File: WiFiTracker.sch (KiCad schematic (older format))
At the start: 30 parts, among them IC1 CP2104, P1 ANT, P2 Battery, P3 USB_B, Q1 MMBT2222A, Q2 MMBT2222A, SW1 SW_RESET, U1 RFM95W-868S2, U2 AP2114, U3 MCP73831T-2ATI/OT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

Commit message: Check PCB V0.1
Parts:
- P3: symbol USB_B -> USB_B-RESCUE-WiFiTracker
- U1: footprint TIH:XCVR_RFM95W-868S2 -> rfm95:XCVR_RFM95W-868S2
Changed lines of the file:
@@
 GPIO0
 $Comp
-L USB_B P3
+L USB_B-RESCUE-WiFiTracker P3
 U 1 1 58AB3572
 P 4320 5825
@@
 F 0 "U1" H 1490 2230 50  0000 L CNN
 F 1 "RFM95W-868S2" H 1490 980 50  0000 L CNN
-F 2 "TIH:XCVR_RFM95W-868S2" H 2090 1680 50  0001 L CNN
+F 2 "rfm95:XCVR_RFM95W-868S2" H 2090 1680 50  0001 L CNN
 F 3 "Mod Txrx Lora +20dbm 868mhz Smd" H 2090 1680 50  0001 L CNN
 F 4 "22.89 USD" H 2090 1680 50  0001 L CNN "Price"

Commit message: Added pin DIOs
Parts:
- added D6, D7, D8: D, symbol D
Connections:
- net RST_RN is gone; now on net RESET: U4.4 (GPIO16)
- net SCL is gone; now on net GPIO5: U4.20 (GPIO5)
- net SRX is gone; now on net GPIO12: U4.6 (GPIO12)
- net STX is gone; now on net GPIO14: U4.5 (GPIO14)
- net GPIO15: now also D6.1 (K), D7.1 (K), D8.1 (K)
- net DIO0: now reaches U1.14 (DIO0)
- net DIO0: now also D7.2 (A)
- net DIO1: now reaches U1.15 (DIO1)
- net DIO1: now also D8.2 (A)
- net DIO2: now reaches U1.16 (DIO2)
- net DIO2: now also D6.2 (A)
- net GPIO16 renamed GPIO5
- net SDA renamed GPIO4
- no-connect marks 27 -> 25
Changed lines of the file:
@@
 $EndComp
 $Comp
-L GND #PWR01
+L GND #PWR5
 U 1 1 58AB3534
 P 995 5905
-F 0 "#PWR01" H 995 5655 50  0001 C CNN
+F 0 "#PWR5" H 995 5655 50  0001 C CNN
 F 1 "GND" H 995 5755 50  0000 C CNN
 F 2 "" H 995 5905 50  0000 C CNN
@@
 $EndComp
 $Comp
-L +3.3V #PWR02
+L +3.3V #PWR7
 U 1 1 58AB3536
 P 2895 5305
-F 0 "#PWR02" H 2895 5155 50  0001 C CNN
+F 0 "#PWR7" H 2895 5155 50  0001 C CNN
 F 1 "+3.3V" H 2895 5445 50  0000 C CNN
 F 2 "" H 2895 5305 50  0000 C CNN
@@
 $EndComp
 $Comp
-L VCC #PWR03
+L VCC #PWR1
 U 1 1 58AB3537
 P 595 4855
-F 0 "#PWR03" H 595 4705 50  0001 C CNN
+F 0 "#PWR1" H 595 4705 50  0001 C CNN
 F 1 "VCC" H 595 5005 50  0000 C CNN
 F 2 "" H 595 4855 50  0000 C CNN
@@
 $EndComp
 $Comp
-L +BATT #PWR04
+L +BATT #PWR4
 U 1 1 58AB3538
 P 695 5005
-F 0 "#PWR04" H 695 4855 50  0001 C CNN
+F 0 "#PWR4" H 695 4855 50  0001 C CNN
 F 1 "+BATT" H 695 5145 50  0000 C CNN
 F 2 "" H 695 5005 50  0000 C CNN
@@
 $EndComp
 $Comp
-L GND #PWR05
+L GND #PWR10
 U 1 1 58AB353B
 P 3285 7405
-F 0 "#PWR05" H 3285 7155 50  0001 C CNN
+F 0 "#PWR10" H 3285 7155 50  0001 C CNN
 F 1 "GND" H 3285 7255 50  0000 C CNN
 F 2 "" H 3285 7405 50  0000 C CNN
@@
 $EndComp
 $Comp
-L VCC #PWR06
+L VCC #PWR2
 U 1 1 58AB353C
 P 685 6655
-F 0 "#PWR06" H 685 6505 50  0001 C CNN
+F 0 "#PWR2" H 685 6505 50  0001 C CNN
 F 1 "VCC" H 685 6805 50  0000 C CNN
 F 2 "" H 685 6655 50  0000 C CNN
@@
 $EndComp
 $Comp
-L +BATT #PWR07
+L +BATT #PWR11
 U 1 1 58AB3540
 P 3585 6605
-F 0 "#PWR07" H 3585 6455 50  0001 C CNN
+F 0 "#PWR11" H 3585 6455 50  0001 C CNN
 F 1 "+BATT" H 3585 6745 50  0000 C CNN
 F 2 "" H 3585 6605 50  0000 C CNN
@@
 $EndComp
 $Comp
-L GND #PWR08
+L GND #PWR12
 U 1 1 58AB3541
 P 3635 7155
-F 0 "#PWR08" H 3635 6905 50  0001 C CNN
+F 0 "#PWR12" H 3635 6905 50  0001 C CNN
 F 1 "GND" H 3635 7005 50  0000 C CNN
 F 2 "" H 3635 7155 50  0000 C CNN
@@
 $EndComp
 $Comp
-L GND #PWR09
+L GND #PWR3
 U 1 1 58AB3544
 P 685 7355
-F 0 "#PWR09" H 685 7105 50  0001 C CNN
+F 0 "#PWR3" H 685 7105 50  0001 C CNN
 F 1 "GND" H 685 7205 50  0000 C CNN
 F 2 "" H 685 7355 50  0000 C CNN
@@
 $EndComp
 $Comp
-L GND #PWR010
+L GND #PWR20
 U 1 1 58AB354A
 P 8030 3810
-F 0 "#PWR010" H 8030 3560 50  0001 C CNN
+F 0 "#PWR20" H 8030 3560 50  0001 C CNN
 F 1 "GND" H 8030 3660 50  0000 C CNN
 F 2 "" H 8030 3810 50  0000 C CNN
@@
 $EndComp
 $Comp
-L +3.3V #PWR011
+L +3.3V #PWR21
 U 1 1 58AB354C
 P 8930 3160
-F 0 "#PWR011" H 8930 3010 50  0001 C CNN
+F 0 "#PWR21" H 8930 3010 50  0001 C CNN
 F 1 "+3.3V" H 8930 3300 50  0000 C CNN
 F 2 "" H 8930 3160 50  0000 C CNN
@@
 BATTERY AND SOURCE
 $Comp
-L GND #PWR012
+L GND #PWR6
 U 1 1 58AB355C
 P 2795 5805
-F 0 "#PWR012" H 2795 5555 50  0001 C CNN
+F 0 "#PWR6" H 2795 5555 50  0001 C CNN
 F 1 "GND" H 2795 5655 50  0000 C CNN
 F 2 "" H 2795 5805 50  0000 C CNN
@@
 RXD
 Text Label 9925 1385 0    60   ~ 0
-SCL
+GPIO5
 Text Label 9925 1485 0    60   ~ 0
-SDA
+GPIO4
 NoConn ~ 8955 2385
 NoConn ~ 8855 2385
@@
 CH_PD
 Text Label 7590 1485 2    60   ~ 0
-RST_RN
+RESET
 Text Label 7625 1585 2    60   ~ 0
-STX
+GPIO14
 Text Label 7605 1685 2    60   ~ 0
-SRX
+GPIO12
 Text Label 7615 1785 0    60   ~ 0
 GPIO13
@@
 RESET
 $Comp
-L GND #PWR013
+L GND #PWR22
 U 1 1 58AB355F
 P 9925 1885
-F 0 "#PWR013" H 9925 1635 50  0001 C CNN
+F 0 "#PWR22" H 9925 1635 50  0001 C CNN
 F 1 "GND" H 9925 1735 50  0000 C CNN
 F 2 "" H 9925 1885 50  0000 C CNN
@@
 $EndComp
 $Comp
-L +3.3V #PWR014
+L +3.3V #PWR18
 U 1 1 58AB3560
 P 7425 1885
-F 0 "#PWR014" H 7425 1735 50  0001 C CNN
+F 0 "#PWR18" H 7425 1735 50  0001 C CNN
 F 1 "+3.3V" H 7425 2025 50  0000 C CNN
 F 2 "" H 7425 1885 50  0000 C CNN
@@
 $EndComp
 $Comp
-L GND #PWR015
+L GND #PWR24
 U 1 1 58AB3563
 P 10575 4240
-F 0 "#PWR015" H 10575 3990 50  0001 C CNN
+F 0 "#PWR24" H 10575 3990 50  0001 C CNN
 F 1 "GND" H 10575 4090 50  0000 C CNN
 F 2 "" H 10575 4240 50  0000 C CNN
@@
 $EndComp
 $Comp
-L +3.3V #PWR016
+L +3.3V #PWR23
 U 1 1 58AB3564
 P 10275 3580
-F 0 "#PWR016" H 10275 3430 50  0001 C CNN
+F 0 "#PWR23" H 10275 3430 50  0001 C CNN
 F 1 "+3.3V" H 10275 3720 50  0000 C CNN
 F 2 "" H 10275 3580 50  0000 C CNN
@@
 GPIO2
 $Comp
-L +3.3V #PWR017
+L +3.3V #PWR25
 U 1 1 58AB356D
 P 10895 3565
-F 0 "#PWR017" H 10895 3415 50  0001 C CNN
+F 0 "#PWR25" H 10895 3415 50  0001 C CNN
 F 1 "+3.3V" H 10895 3705 50  0000 C CNN
 F 2 "" H 10895 3565 50  0000 C CNN
@@
 $EndComp
 $Comp
-L +3.3V #PWR018
+L +3.3V #PWR19
 U 1 1 58AB3571
 P 7495 4085
-F 0 "#PWR018" H 7495 3935 50  0001 C CNN
+F 0 "#PWR19" H 7495 3935 50  0001 C CNN
 F 1 "+3.3V" H 7495 4225 50  0000 C CNN
 F 2 "" H 7495 4085 50  0000 C CNN
@@
 NoConn ~ 5075 6420
 $Comp
-L +3.3V #PWR019
+L +3.3V #PWR15
 U 1 1 58AB3574
 P 4855 6215
-F 0 "#PWR019" H 4855 6065 50  0001 C CNN
+F 0 "#PWR15" H 4855 6065 50  0001 C CNN
 F 1 "+3.3V" H 4855 6355 50  0000 C CNN
 F 2 "" H 4855 6215 50  0000 C CNN
@@
 $EndComp
 $Comp
-L GND #PWR020
+L GND #PWR16
 U 1 1 58AB3576
 P 4905 6550
-F 0 "#PWR020" H 4905 6300 50  0001 C CNN
+F 0 "#PWR16" H 4905 6300 50  0001 C CNN
 F 1 "GND" H 4905 6400 50  0000 C CNN
 F 2 "" H 4905 6550 50  0000 C CNN
@@
 NoConn ~ 6475 6320
 $Comp
-L GND #PWR021
+L GND #PWR17
 U 1 1 58AB3577
 P 5010 7110
-F 0 "#PWR021" H 5010 6860 50  0001 C CNN
+F 0 "#PWR17" H 5010 6860 50  0001 C CNN
 F 1 "GND" H 5010 6960 50  0000 C CNN
 F 2 "" H 5010 7110 50  0000 C CNN
@@
 RST
 $Comp
-L VCC #PWR022
+L VCC #PWR13
 U 1 1 58AB3578
 P 4575 6245
-F 0 "#PWR022" H 4575 6095 50  0001 C CNN
+F 0 "#PWR13" H 4575 6095 50  0001 C CNN
 F 1 "VCC" H 4575 6395 50  0000 C CNN
 F 2 "" H 4575 6245 50  0000 C CNN
@@
 $EndComp
 $Comp
-L GND #PWR023
+L GND #PWR14
 U 1 1 58AB3579
 P 4785 5590
-F 0 "#PWR023" H 4785 5340 50  0001 C CNN
+F 0 "#PWR14" H 4785 5340 50  0001 C CNN
 F 1 "GND" H 4785 5440 50  0000 C CNN
 F 2 "" H 4785 5590 50  0000 C CNN
@@
 GPIO14
 Text Label 1180 1480 2    60   ~ 0
-GPIO16
-$Comp
-L GND #PWR024
+GPIO5
+$Comp
+L GND #PWR8
 U 1 1 58AB7D79
 P 2960 2370
-F 0 "#PWR024" H 2960 2120 50  0001 C CNN
+F 0 "#PWR8" H 2960 2120 50  0001 C CNN
 F 1 "GND" H 2960 2220 50  0000 C CNN
 F 2 "" H 2960 2370 50  0000 C CNN
@@
 $EndComp
 $Comp
-L +3.3V #PWR025
+L +3.3V #PWR9
 U 1 1 58AB7DFC
 P 3040 1210
-F 0 "#PWR025" H 3040 1060 50  0001 C CNN
+F 0 "#PWR9" H 3040 1060 50  0001 C CNN
 F 1 "+3.3V" H 3040 1350 50  0000 C CNN
 F 2 "" H 3040 1210 50  0000 C CNN
@@
 	1    0    0    -1
 $EndComp
-NoConn ~ 1390 2180
-NoConn ~ 1390 2080
-NoConn ~ 1390 1980
 NoConn ~ 1390 1880
 NoConn ~ 1390 1780
@@
 	1    590  5200
 	0    -1   -1   0
+$EndComp
+NoConn ~ 2595 5755
+$Comp
+L CONN_01X01 P1
+U 1 1 58AC21D1
+P 3410 1480
+F 0 "P1" H 3410 1580 50  0000 C CNN
+F 1 "ANT" V 3510 1480 50  0000 C CNN
+F 2 "Connect:1pin" H 3410 1480 50  0001 C CNN
+F 3 "" H 3410 1480 50  0000 C CNN
+	1    3410 1480
+	1    0    0    -1
+$EndComp
+NoConn ~ 1645 5605
+Text Label 1285 1980 2    60   ~ 0
+DIO0
+Text Label 1285 2080 2    60   ~ 0
+DIO1
+Text Label 1280 2180 2    60   ~ 0
+DIO2
+NoConn ~ 1390 1580
+$Comp
+L D D8
+U 1 1 5940BAF2
+P 5705 935
+F 0 "D8" H 5705 1035 50  0000 C CNN
+F 1 "D" H 5705 835 50  0000 C CNN
+F 2 "" H 5705 935 50  0000 C CNN
+F 3 "" H 5705 935 50  0000 C CNN
+	1    5705 935
+	-1   0    0    1
+$EndComp
+$Comp
+L D D6
+U 1 1 5940BBBD
+P 5690 1205
+F 0 "D6" H 5690 1305 50  0000 C CNN
+F 1 "D" H 5690 1105 50  0000 C CNN
+F 2 "" H 5690 1205 50  0000 C CNN
+F 3 "" H 5690 1205 50  0000 C CNN
+	1    5690 1205
+	-1   0    0    1
+$EndComp
+$Comp
+L D D7
+U 1 1 5940BDF7
+P 5695 660
+F 0 "D7" H 5695 760 50  0000 C CNN
+F 1 "D" H 5695 560 50  0000 C CNN
+F 2 "" H 5695 660 50  0000 C CNN
+F 3 "" H 5695 660 50  0000 C CNN
+	1    5695 660
+	-1   0    0    1
 $EndComp
 Wire Wire Line
@@
 	5415 3255 5290 3255
 Wire Wire Line
-	5090 3255 4890 3255
+	4890 3255 5090 3255
 Wire Wire Line
 	5400 2630 5275 2630
 Wire Wire Line
-	5075 2630 4875 2630
+	4875 2630 5075 2630
 Wire Wire Line
 	5700 2830 5700 2915
@@
 	695  5355 695  5405
 Connection ~ 695  5405
-NoConn ~ 2595 5755
-$Comp
-L CONN_01X01 P1
-U 1 1 58AC21D1
-P 3410 1480
-F 0 "P1" H 3410 1580 50  0000 C CNN
-F 1 "ANT" V 3510 1480 50  0000 C CNN
-F 2 "Connect:1pin" H 3410 1480 50  0001 C CNN
-F 3 "" H 3410 1480 50  0000 C CNN
-	1    3410 1480
-	1    0    0    -1
-$EndComp
 Wire Wire Line
 	2790 1480 3210 1480
-NoConn ~ 1645 5605
+Wire Wire Line
+	1390 1980 1285 1980
+Wire Wire Line
+	1390 2080 1285 2080
+Wire Wire Line
+	1390 2180 1280 2180
+Wire Wire Line
+	5845 660  5965 660
+Wire Wire Line
+	5965 660  5965 1205
+Wire Wire Line
+	5965 1205 5840 1205
+Wire Wire Line
+	5855 935  6210 935
+Connection ~ 5965 935
+Wire Wire Line
+	5545 660  5370 660
+Wire Wire Line
+	5555 935  5380 935
+Wire Wire Line
+	5540 1205 5395 1205
+Text Label 5370 660  0    60   ~ 0
+DIO0
+Text Label 5380 935  0    60   ~ 0
+DIO1
+Text Label 5395 1205 0    60   ~ 0
+DIO2
+Text Label 6210 935  0    60   ~ 0
+GPIO15
 $EndSCHEMATC

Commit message: Update name
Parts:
- D6, D7, D8: footprint (none) -> Diodes_SMD:D_SOD-123F
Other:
- note added: "RFM95"
- note removed: "RN2903 LoRa"
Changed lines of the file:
@@
 Title "LoRaCat: WiFiTracker"
 Date "2017-02-20"
-Rev "0.1"
+Rev "0.2"
 Comp "Electronic Cats"
 Comment1 "Andres Sabas"
@@
 $EndComp
 $Comp
-L GND #PWR5
+L GND #PWR01
 U 1 1 58AB3534
 P 995 5905
-F 0 "#PWR5" H 995 5655 50  0001 C CNN
+F 0 "#PWR01" H 995 5655 50  0001 C CNN
 F 1 "GND" H 995 5755 50  0000 C CNN
 F 2 "" H 995 5905 50  0000 C CNN
@@
 $EndComp
 $Comp
-L +3.3V #PWR7
+L +3.3V #PWR02
 U 1 1 58AB3536
 P 2895 5305
-F 0 "#PWR7" H 2895 5155 50  0001 C CNN
+F 0 "#PWR02" H 2895 5155 50  0001 C CNN
 F 1 "+3.3V" H 2895 5445 50  0000 C CNN
 F 2 "" H 2895 5305 50  0000 C CNN
@@
 $EndComp
 $Comp
-L VCC #PWR1
+L VCC #PWR03
 U 1 1 58AB3537
 P 595 4855
-F 0 "#PWR1" H 595 4705 50  0001 C CNN
+F 0 "#PWR03" H 595 4705 50  0001 C CNN
 F 1 "VCC" H 595 5005 50  0000 C CNN
 F 2 "" H 595 4855 50  0000 C CNN
@@
 $EndComp
 $Comp
-L +BATT #PWR4
+L +BATT #PWR04
 U 1 1 58AB3538
 P 695 5005
-F 0 "#PWR4" H 695 4855 50  0001 C CNN
+F 0 "#PWR04" H 695 4855 50  0001 C CNN
 F 1 "+BATT" H 695 5145 50  0000 C CNN
 F 2 "" H 695 5005 50  0000 C CNN
@@
 $EndComp
 $Comp
-L GND #PWR10
+L GND #PWR05
 U 1 1 58AB353B
 P 3285 7405
-F 0 "#PWR10" H 3285 7155 50  0001 C CNN
+F 0 "#PWR05" H 3285 7155 50  0001 C CNN
 F 1 "GND" H 3285 7255 50  0000 C CNN
 F 2 "" H 3285 7405 50  0000 C CNN
@@
 $EndComp
 $Comp
-L VCC #PWR2
+L VCC #PWR06
 U 1 1 58AB353C
 P 685 6655
-F 0 "#PWR2" H 685 6505 50  0001 C CNN
+F 0 "#PWR06" H 685 6505 50  0001 C CNN
 F 1 "VCC" H 685 6805 50  0000 C CNN
 F 2 "" H 685 6655 50  0000 C CNN
@@
 $EndComp
 $Comp
-L +BATT #PWR11
+L +BATT #PWR07
 U 1 1 58AB3540
 P 3585 6605
-F 0 "#PWR11" H 3585 6455 50  0001 C CNN
+F 0 "#PWR07" H 3585 6455 50  0001 C CNN
 F 1 "+BATT" H 3585 6745 50  0000 C CNN
 F 2 "" H 3585 6605 50  0000 C CNN
@@
 $EndComp
 $Comp
-L GND #PWR12
+L GND #PWR08
 U 1 1 58AB3541
 P 3635 7155
-F 0 "#PWR12" H 3635 6905 50  0001 C CNN
+F 0 "#PWR08" H 3635 6905 50  0001 C CNN
 F 1 "GND" H 3635 7005 50  0000 C CNN
 F 2 "" H 3635 7155 50  0000 C CNN
@@
 $EndComp
 $Comp
-L GND #PWR3
+L GND #PWR09
 U 1 1 58AB3544
 P 685 7355
-F 0 "#PWR3" H 685 7105 50  0001 C CNN
+F 0 "#PWR09" H 685 7105 50  0001 C CNN
 F 1 "GND" H 685 7205 50  0000 C CNN
 F 2 "" H 685 7355 50  0000 C CNN
@@
 $EndComp
 $Comp
-L GND #PWR20
+L GND #PWR010
 U 1 1 58AB354A
 P 8030 3810
-F 0 "#PWR20" H 8030 3560 50  0001 C CNN
+F 0 "#PWR010" H 8030 3560 50  0001 C CNN
 F 1 "GND" H 8030 3660 50  0000 C CNN
 F 2 "" H 8030 3810 50  0000 C CNN
@@
 $EndComp
 $Comp
-L +3.3V #PWR21
+L +3.3V #PWR011
 U 1 1 58AB354C
 P 8930 3160
-F 0 "#PWR21" H 8930 3010 50  0001 C CNN
+F 0 "#PWR011" H 8930 3010 50  0001 C CNN
 F 1 "+3.3V" H 8930 3300 50  0000 C CNN
 F 2 "" H 8930 3160 50  0000 C CNN
@@
 RST
 Text Notes 1600 600  0    60   ~ 0
-RN2903 LoRa
+RFM95
 Text Notes 9405 690  0    60   ~ 0
 ESP8266
@@
 BATTERY AND SOURCE
 $Comp
-L GND #PWR6
+L GND #PWR012
 U 1 1 58AB355C
 P 2795 5805
-F 0 "#PWR6" H 2795 5555 50  0001 C CNN
+F 0 "#PWR012" H 2795 5555 50  0001 C CNN
 F 1 "GND" H 2795 5655 50  0000 C CNN
 F 2 "" H 2795 5805 50  0000 C CNN
@@
 RESET
 $Comp
-L GND #PWR22
+L GND #PWR013
 U 1 1 58AB355F
 P 9925 1885
-F 0 "#PWR22" H 9925 1635 50  0001 C CNN
+F 0 "#PWR013" H 9925 1635 50  0001 C CNN
 F 1 "GND" H 9925 1735 50  0000 C CNN
 F 2 "" H 9925 1885 50  0000 C CNN
@@
 $EndComp
 $Comp
-L +3.3V #PWR18
+L +3.3V #PWR014
 U 1 1 58AB3560
 P 7425 1885
-F 0 "#PWR18" H 7425 1735 50  0001 C CNN
+F 0 "#PWR014" H 7425 1735 50  0001 C CNN
 F 1 "+3.3V" H 7425 2025 50  0000 C CNN
 F 2 "" H 7425 1885 50  0000 C CNN
@@
 $EndComp
 $Comp
-L GND #PWR24
+L GND #PWR015
 U 1 1 58AB3563
 P 10575 4240
-F 0 "#PWR24" H 10575 3990 50  0001 C CNN
+F 0 "#PWR015" H 10575 3990 50  0001 C CNN
 F 1 "GND" H 10575 4090 50  0000 C CNN
 F 2 "" H 10575 4240 50  0000 C CNN
@@
 $EndComp
 $Comp
-L +3.3V #PWR23
+L +3.3V #PWR016
 U 1 1 58AB3564
 P 10275 3580
-F 0 "#PWR23" H 10275 3430 50  0001 C CNN
+F 0 "#PWR016" H 10275 3430 50  0001 C CNN
 F 1 "+3.3V" H 10275 3720 50  0000 C CNN
 F 2 "" H 10275 3580 50  0000 C CNN
@@
 GPIO2
 $Comp
-L +3.3V #PWR25
+L +3.3V #PWR017
 U 1 1 58AB356D
 P 10895 3565
-F 0 "#PWR25" H 10895 3415 50  0001 C CNN
+F 0 "#PWR017" H 10895 3415 50  0001 C CNN
 F 1 "+3.3V" H 10895 3705 50  0000 C CNN
 F 2 "" H 10895 3565 50  0000 C CNN
@@
 $EndComp
 $Comp
-L +3.3V #PWR19
+L +3.3V #PWR018
 U 1 1 58AB3571
 P 7495 4085
-F 0 "#PWR19" H 7495 3935 50  0001 C CNN
+F 0 "#PWR018" H 7495 3935 50  0001 C CNN
 F 1 "+3.3V" H 7495 4225 50  0000 C CNN
 F 2 "" H 7495 4085 50  0000 C CNN
@@
 NoConn ~ 5075 6420
 $Comp
-L +3.3V #PWR15
+L +3.3V #PWR019
 U 1 1 58AB3574
 P 4855 6215
-F 0 "#PWR15" H 4855 6065 50  0001 C CNN
+F 0 "#PWR019" H 4855 6065 50  0001 C CNN
 F 1 "+3.3V" H 4855 6355 50  0000 C CNN
 F 2 "" H 4855 6215 50  0000 C CNN
@@
 $EndComp
 $Comp
-L GND #PWR16
+L GND #PWR020
 U 1 1 58AB3576
 P 4905 6550
-F 0 "#PWR16" H 4905 6300 50  0001 C CNN
+F 0 "#PWR020" H 4905 6300 50  0001 C CNN
 F 1 "GND" H 4905 6400 50  0000 C CNN
 F 2 "" H 4905 6550 50  0000 C CNN
@@
 NoConn ~ 6475 6320
 $Comp
-L GND #PWR17
+L GND #PWR021
 U 1 1 58AB3577
 P 5010 7110
-F 0 "#PWR17" H 5010 6860 50  0001 C CNN
+F 0 "#PWR021" H 5010 6860 50  0001 C CNN
 F 1 "GND" H 5010 6960 50  0000 C CNN
 F 2 "" H 5010 7110 50  0000 C CNN
@@
 RST
 $Comp
-L VCC #PWR13
+L VCC #PWR022
 U 1 1 58AB3578
 P 4575 6245
-F 0 "#PWR13" H 4575 6095 50  0001 C CNN
+F 0 "#PWR022" H 4575 6095 50  0001 C CNN
 F 1 "VCC" H 4575 6395 50  0000 C CNN
 F 2 "" H 4575 6245 50  0000 C CNN
@@
 $EndComp
 $Comp
-L GND #PWR14
+L GND #PWR023
 U 1 1 58AB3579
 P 4785 5590
-F 0 "#PWR14" H 4785 5340 50  0001 C CNN
+F 0 "#PWR023" H 4785 5340 50  0001 C CNN
 F 1 "GND" H 4785 5440 50  0000 C CNN
 F 2 "" H 4785 5590 50  0000 C CNN
@@
 GPIO5
 $Comp
-L GND #PWR8
+L GND #PWR024
 U 1 1 58AB7D79
 P 2960 2370
-F 0 "#PWR8" H 2960 2120 50  0001 C CNN
+F 0 "#PWR024" H 2960 2120 50  0001 C CNN
 F 1 "GND" H 2960 2220 50  0000 C CNN
 F 2 "" H 2960 2370 50  0000 C CNN
@@
 $EndComp
 $Comp
-L +3.3V #PWR9
+L +3.3V #PWR025
 U 1 1 58AB7DFC
 P 3040 1210
-F 0 "#PWR9" H 3040 1060 50  0001 C CNN
+F 0 "#PWR025" H 3040 1060 50  0001 C CNN
 F 1 "+3.3V" H 3040 1350 50  0000 C CNN
 F 2 "" H 3040 1210 50  0000 C CNN
@@
 F 0 "D8" H 5705 1035 50  0000 C CNN
 F 1 "D" H 5705 835 50  0000 C CNN
-F 2 "" H 5705 935 50  0000 C CNN
+F 2 "Diodes_SMD:D_SOD-123F" H 5705 935 50  0001 C CNN
 F 3 "" H 5705 935 50  0000 C CNN
 	1    5705 935
@@
 F 0 "D6" H 5690 1305 50  0000 C CNN
 F 1 "D" H 5690 1105 50  0000 C CNN
-F 2 "" H 5690 1205 50  0000 C CNN
+F 2 "Diodes_SMD:D_SOD-123F" H 5690 1205 50  0001 C CNN
 F 3 "" H 5690 1205 50  0000 C CNN
 	1    5690 1205
@@
 F 0 "D7" H 5695 760 50  0000 C CNN
 F 1 "D" H 5695 560 50  0000 C CNN
-F 2 "" H 5695 660 50  0000 C CNN
+F 2 "Diodes_SMD:D_SOD-123F" H 5695 660 50  0001 C CNN
 F 3 "" H 5695 660 50  0000 C CNN
 	1    5695 660

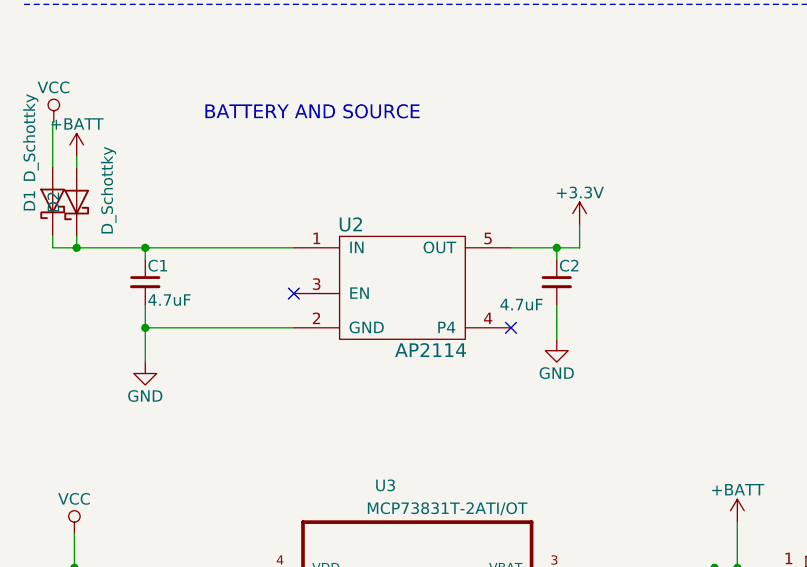
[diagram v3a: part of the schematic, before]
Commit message: Added Lib AP2114
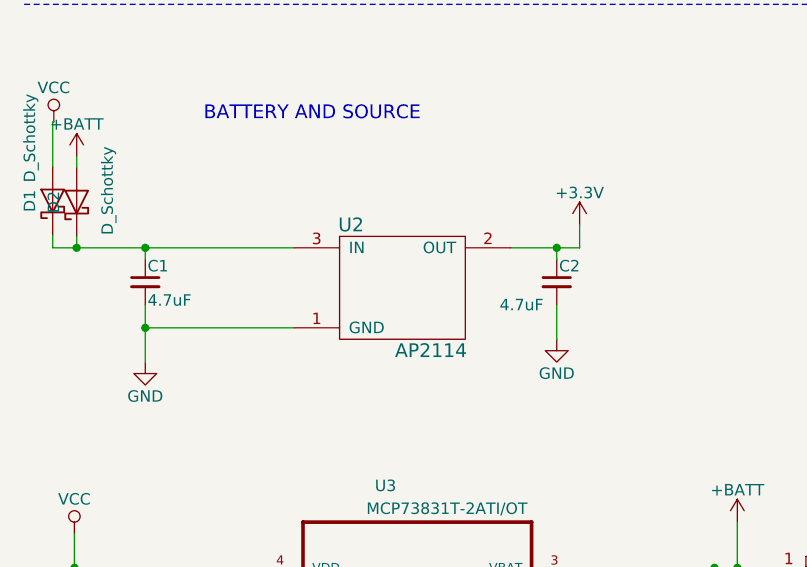
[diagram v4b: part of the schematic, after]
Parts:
- removed U2: AP2114, TO_SOT_Packages_SMD:SOT-223-3Lead_TabPin2, symbol AP2112
- added U2: AP2114, TO_SOT_Packages_SMD:SOT-223-3Lead_TabPin2, symbol AP2112-RESCUE-NodeLoRaGroveKitty
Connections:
- net +3V3: now also U2.2 (OUT)
- net GND: now also U2.1 (GND)
- net at C1.1, D1.1 (K), D2.1 (K): now also U2.3 (IN)
- no-connect marks 25 -> 23
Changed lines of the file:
@@
 Title "LoRaCat: WiFiTracker"
 Date "2017-02-20"
-Rev "0.2"
+Rev "0.3"
 Comp "Electronic Cats"
 Comment1 "Andres Sabas"
@@
 Comment4 ""
 $EndDescr
-$Comp
-L AP2112 U2
-U 1 1 58AB3530
-P 2095 5605
-F 0 "U2" H 1895 5905 60  0000 C CNN
-F 1 "AP2114" H 2245 5355 60  0000 C CNN
-F 2 "TO_SOT_Packages_SMD:SOT-223-3Lead_TabPin2" H 2095 5605 60  0001 C CNN
-F 3 "" H 2095 5605 60  0000 C CNN
-F 4 "AP2114H-3.3TRG1" H 2095 5605 60  0001 C CNN "manf#"
-	1    2095 5605
-	1    0    0    -1
-$EndComp
 $Comp
 L C_Small C1
@@
 	0    -1   -1   0
 $EndComp
-NoConn ~ 2595 5755
 $Comp
 L CONN_01X01 P1
@@
 	1    0    0    -1
 $EndComp
-NoConn ~ 1645 5605
 Text Label 1285 1980 2    60   ~ 0
 DIO0
@@
 Text Label 6210 935  0    60   ~ 0
 GPIO15
+$Comp
+L AP2112-RESCUE-NodeLoRaGroveKitty U2
+U 1 1 5940AB22
+P 2095 5605
+F 0 "U2" H 1895 5905 60  0000 C CNN
+F 1 "AP2114" H 2245 5355 60  0000 C CNN
+F 2 "TO_SOT_Packages_SMD:SOT-223-3Lead_TabPin2" H 2095 5605 60  0001 C CNN
+F 3 "" H 2095 5605 60  0000 C CNN
+	1    2095 5605
+	1    0    0    -1
+$EndComp
 $EndSCHEMATC
